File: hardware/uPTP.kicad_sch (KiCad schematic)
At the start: 1 part, among them U1 CH32V30xWxUx

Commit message: Key components
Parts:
- removed U1: CH32V30xWxUx, Package_DFN_QFN:QFN-68-1EP_8x8mm_P0.4mm_EP6.4x6.4mm, symbol MCU_WCH_CH32V3:CH32V30xWxUx
- added J1: USB_C_Receptacle_USB2.0_14P, symbol Connector:USB_C_Receptacle_USB2.0_14P
- added U1: CH32V307WCU6, uPTP:QFN-68_L8.0-W8.0-P0.40-BL-EP6.7, symbol uPTP:CH32V30xWxUx
- added U2: HC-RJ45-055-7, uPTP:RJ45-SMD_HC-RJ45-055-7_1, symbol uPTP:HC-RJ45-055-7
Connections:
- new net: J1.A1 (GND), J1.A12 (GND), J1.B1 (GND), J1.B12 (GND)
- new net: J1.A4 (VBUS), J1.A9 (VBUS), J1.B4 (VBUS), J1.B9 (VBUS)
- new net: U1.17 (VIO), U1.31 (VIO), U1.51 (VIO), U1.67 (VIO)
- new net: U1.18 (VSS), U1.49 (VSS), U1.69 (VSS)
- new net: U1.32 (VDD), U1.50 (VDD), U1.68 (VDD)
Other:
- note added: "TODO check exposed pad!"

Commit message: Some more handy components
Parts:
- removed J1: USB_C_Receptacle_USB2.0_14P, symbol Connector:USB_C_Receptacle_USB2.0_14P
- added D1: USBLC6-2SC6, uPTP:SOT-23-6_L2.9-W1.6-P0.95-LS2.8-BL, symbol uPTP:USBLC6-2SC6
- added J2: SMA, symbol Connector:Conn_Coaxial
- added J3: u.FL, symbol Connector:Conn_Coaxial_Small
- added USB1: TYPE-C 16PIN 2MD(073), uPTP:USB-C-SMD_TYPE-C-16PIN, symbol uPTP:USB-C-SMD_TYPE-C-16PIN
- added Y1: Crystal_GND2_Small, symbol Device:Crystal_GND2_Small
- U1: LCSC Part (none) -> C5142795
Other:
- note removed: "TODO check exposed pad!"
- moved on the sheet: U2

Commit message: Add magnetics
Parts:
- added TR1: ~, uPTP:B1608S, symbol uPTP:B1608S
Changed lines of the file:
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@@
+	)
+	(symbol
+		(lib_id "uPTP:B1608S")
+		(at 218.44 120.65 0)
+		(unit 1)
+		(exclude_from_sim no)
+		(in_bom yes)
+		(on_board yes)
+		(dnp no)
+		(property "Reference" "TR1"
+			(at 218.44 108.966 0)
+			(effects
+				(font
+					(size 1.27 1.27)
+				)
+			)
+		)
+		(property "Value" "~"
+			(at 218.44 109.22 0)
+			(effects
+				(font
+					(size 1.27 1.27)
+				)
+			)
+		)
+		(property "Footprint" "uPTP:B1608S"
+			(at 218.44 135.128 0)
+			(effects
+				(font
+					(size 1.27 1.27)
+				)
+				(hide yes)
+			)
+		)
+		(property "Datasheet" ""
+			(at 218.44 109.22 0)
+			(effects
+				(font
+					(size 1.27 1.27)
+				)
+				(hide yes)
+			)
+		)
+		(property "Description" "POE-Rated (720mA) Ethernet Magnetics"
+			(at 218.186 132.588 0)
+			(effects
+				(font
+					(size 1.27 1.27)
+				)
+				(hide yes)
+			)
+		)
+		(property "LCSC Part" "C507596"
+			(at 218.44 137.414 0)
+			(effects
+				(font
+					(size 1.27 1.27)
+				)
+				(hide yes)
+			)
+		)
+		(pin "6"
+		)
+		(pin "9"
+		)
+		(pin "8"
+		)
+		(pin "3"
+		)
+		(pin "11"
+		)
+		(pin "1"
+		)
+		(pin "10"
+		)
+		(pin "7"
+		)
+		(pin "2"
+		)
+		(pin "15"
+		)
+		(pin "14"
+		)
+		(pin "16"
+		)
+		(instances
+			(project ""
+				(path "/c29659fd-9e8d-4714-a690-4e74e6e849c2"
+					(reference "TR1")
+					(unit 1)
+				)
+			)
+		)
 	)
 	(symbol

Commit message: Nice first render
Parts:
- added H1, H2: MountingHole_Pad, MountingHole:MountingHole_3.2mm_M3_Pad, symbol Mechanical:MountingHole_Pad
- added J1: Conn_01x04_Pin, Connector_PinHeader_2.54mm:PinHeader_1x04_P2.54mm_Horizontal, symbol Connector:Conn_01x04_Pin
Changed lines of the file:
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@@
+	)
+	(symbol
+		(lib_id "Mechanical:MountingHole_Pad")
+		(at 107.95 179.07 0)
+		(unit 1)
+		(exclude_from_sim yes)
+		(in_bom no)
+		(on_board yes)
+		(dnp no)
+		(fields_autoplaced yes)
+		(property "Reference" "H1"
+			(at 110.49 176.5299 0)
+			(effects
+				(font
+					(size 1.27 1.27)
+				)
+				(justify left)
+			)
+		)
+		(property "Value" "MountingHole_Pad"
+			(at 110.49 179.0699 0)
+			(effects
+				(font
+					(size 1.27 1.27)
+				)
+				(justify left)
+			)
+		)
+		(property "Footprint" "MountingHole:MountingHole_3.2mm_M3_Pad"
+			(at 107.95 179.07 0)
+			(effects
+				(font
+					(size 1.27 1.27)
+				)
+				(hide yes)
+			)
+		)
+		(property "Datasheet" "~"
+			(at 107.95 179.07 0)
+			(effects
+				(font
+					(size 1.27 1.27)
+				)
+				(hide yes)
+			)
+		)
+		(property "Description" "Mounting Hole with connection"
+			(at 107.95 179.07 0)
+			(effects
+				(font
+					(size 1.27 1.27)
+				)
+				(hide yes)
+			)
+		)
+		(pin "1"
+		)
+		(instances
+			(project ""
+				(path "/c29659fd-9e8d-4714-a690-4e74e6e849c2"
+					(reference "H1")
+					(unit 1)
+				)
+			)
+		)
 	)
 	(symbol
@@
 	)
 	(symbol
+		(lib_id "Mechanical:MountingHole_Pad")
+		(at 127 179.07 0)
+		(unit 1)
+		(exclude_from_sim yes)
+		(in_bom no)
+		(on_board yes)
+		(dnp no)
+		(fields_autoplaced yes)
+		(property "Reference" "H2"
+			(at 129.54 176.5299 0)
+			(effects
+				(font
+					(size 1.27 1.27)
+				)
+				(justify left)
+			)
+		)
+		(property "Value" "MountingHole_Pad"
+			(at 129.54 179.0699 0)
+			(effects
+				(font
+					(size 1.27 1.27)
+				)
+				(justify left)
+			)
+		)
+		(property "Footprint" "MountingHole:MountingHole_3.2mm_M3_Pad"
+			(at 127 179.07 0)
+			(effects
+				(font
+					(size 1.27 1.27)
+				)
+				(hide yes)
+			)
+		)
+		(property "Datasheet" "~"
+			(at 127 179.07 0)
+			(effects
+				(font
+					(size 1.27 1.27)
+				)
+				(hide yes)
+			)
+		)
+		(property "Description" "Mounting Hole with connection"
+			(at 127 179.07 0)
+			(effects
+				(font
+					(size 1.27 1.27)
+				)
+				(hide yes)
+			)
+		)
+		(pin "1"
+		)
+		(instances
+			(project "uPTP"
+				(path "/c29659fd-9e8d-4714-a690-4e74e6e849c2"
+					(reference "H2")
+					(unit 1)
+				)
+			)
+		)
+	)
+	(symbol
 		(lib_id "uPTP:USBLC6-2SC6")
 		(at 80.01 74.93 0)
@@
 					(unit 1)
 				)
+			)
+		)
+	)
+	(symbol
+		(lib_id "Connector:Conn_01x04_Pin")
+		(at 45.72 123.19 0)
+		(unit 1)
+		(exclude_from_sim no)
+		(in_bom yes)
+		(on_board yes)
+		(dnp no)
+		(fields_autoplaced yes)
+		(property "Reference" "J1"
+			(at 46.355 115.57 0)
+			(effects
+				(font
+					(size 1.27 1.27)
+				)
+			)
+		)
+		(property "Value" "Conn_01x04_Pin"
+			(at 46.355 118.11 0)
+			(effects
+				(font
+					(size 1.27 1.27)
+				)
+			)
+		)
+		(property "Footprint" "Connector_PinHeader_2.54mm:PinHeader_1x04_P2.54mm_Horizontal"
+			(at 45.72 123.19 0)
+			(effects
+				(font
+					(size 1.27 1.27)
+				)
+				(hide yes)
+			)
+		)
+		(property "Datasheet" "~"
+			(at 45.72 123.19 0)
+			(effects
+				(font
+					(size 1.27 1.27)
+				)
+				(hide yes)
+			)
+		)
+		(property "Description" "Generic connector, single row, 01x04, script generated"
+			(at 45.72 123.19 0)
+			(effects
+				(font
+					(size 1.27 1.27)
+				)
+				(hide yes)
+			)
+		)
+		(pin "4"
+		)
+		(pin "1"
+		)
+		(pin "2"
+		)
+		(pin "3"
+		)
+		(instances
+			(project ""
+				(path "/c29659fd-9e8d-4714-a690-4e74e6e849c2"
+					(reference "J1")
+					(unit 1)
+				)

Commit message: POE CTRL?
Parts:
- added D2: D_Schottky, symbol Device:D_Schottky
- added U3: TMI7301, uPTP:SOP-8_L4.9-W3.9-P1.27-LS6.0-TL, symbol uPTP:TMI7301
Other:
- moved on the sheet: J1, TR1, U1, U2, Y1
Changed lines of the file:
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@@
 	(symbol
 		(lib_id "uPTP:HC-RJ45-055-7")
-		(at 247.65 120.65 0)
+		(at 36.83 152.4 0)
+		(mirror y)
 		(unit 1)
 		(exclude_from_sim no)
@@
 		(on_board yes)
 		(dnp no)
-		(fields_autoplaced yes)
 		(property "Reference" "U2"
-			(at 257.81 119.3799 0)
+			(at 26.67 151.1299 0)
 			(effects
 				(font
@@
 		)
 		(property "Value" "HC-RJ45-055-7"
-			(at 257.81 121.9199 0)
+			(at 26.67 153.6699 0)
 			(effects
 				(font
@@
 		)
 		(property "Footprint" "uPTP:RJ45-SMD_HC-RJ45-055-7_1"
-			(at 247.65 142.24 0)
+			(at 36.83 173.99 0)
 			(effects
 				(font
@@
 		)
 		(property "Datasheet" ""
-			(at 241.3 120.65 0)
+			(at 43.18 152.4 0)
 			(effects
 				(font
@@
 		)
 		(property "Description" "Half-Recessed SMD RJ45 Connector"
-			(at 241.3 120.65 0)
+			(at 43.18 152.4 0)
 			(effects
 				(font
@@
 		)
 		(property "LCSC Part" "C3000213"
-			(at 247.65 144.78 0)
+			(at 36.83 176.53 0)
 			(effects
 				(font
@@
 	(symbol
 		(lib_id "Device:Crystal_GND2_Small")
-		(at 185.42 57.15 0)
+		(at 193.04 97.79 0)
 		(unit 1)
 		(exclude_from_sim no)
@@
 		(fields_autoplaced yes)
 		(property "Reference" "Y1"
-			(at 185.42 50.8 0)
+			(at 193.04 91.44 0)
 			(effects
 				(font
@@
 		)
 		(property "Value" "Crystal_GND2_Small"
-			(at 185.42 53.34 0)
+			(at 193.04 93.98 0)
 			(effects
 				(font
@@
 		)
 		(property "Footprint" ""
-			(at 185.42 57.15 0)
+			(at 193.04 97.79 0)
 			(effects
 				(font
@@
 		)
 		(property "Datasheet" "~"
-			(at 185.42 57.15 0)
+			(at 193.04 97.79 0)
 			(effects
 				(font
@@
 		)
 		(property "Description" "Three pin crystal, GND on pin 2, small symbol"
-			(at 185.42 57.15 0)
+			(at 193.04 97.79 0)
 			(effects
 				(font
@@
 	(symbol
 		(lib_id "uPTP:B1608S")
-		(at 218.44 120.65 0)
+		(at 62.23 152.4 0)
 		(unit 1)
 		(exclude_from_sim no)
@@
 		(dnp no)
 		(property "Reference" "TR1"
-			(at 218.44 108.966 0)
+			(at 62.23 140.716 0)
 			(effects
 				(font
@@
 		)
 		(property "Value" "~"
-			(at 218.44 109.22 0)
+			(at 62.23 140.97 0)
 			(effects
 				(font
@@
 		)
 		(property "Footprint" "uPTP:B1608S"
-			(at 218.44 135.128 0)
+			(at 62.23 166.878 0)
 			(effects
 				(font
@@
 		)
 		(property "Datasheet" ""
-			(at 218.44 109.22 0)
+			(at 62.23 140.97 0)
 			(effects
 				(font
@@
 		)
 		(property "Description" "POE-Rated (720mA) Ethernet Magnetics"
-			(at 218.186 132.588 0)
+			(at 61.976 164.338 0)
 			(effects
 				(font
@@
 		)
 		(property "LCSC Part" "C507596"
-			(at 218.44 137.414 0)
+			(at 62.23 169.164 0)
 			(effects
 				(font
@@
 	(symbol
 		(lib_id "uPTP:CH32V30xWxUx")
-		(at 140.97 106.68 0)
+		(at 152.4 87.63 0)
 		(unit 1)
 		(exclude_from_sim no)
@@
 		(fields_autoplaced yes)
 		(property "Reference" "U1"
-			(at 153.3241 157.48 0)
+			(at 164.7541 138.43 0)
 			(effects
 				(font
@@
 		)
 		(property "Value" "CH32V307WCU6"
-			(at 153.3241 160.02 0)
+			(at 164.7541 140.97 0)
 			(effects
 				(font
@@
 		)
 		(property "Footprint" "uPTP:QFN-68_L8.0-W8.0-P0.40-BL-EP6.7"
-			(at 140.97 101.6 0)
+			(at 152.4 82.55 0)
 			(effects
 				(font
@@
 		)
 		(property "Datasheet" "http://www.wch-ic.com/products/CH32V307.html?"
-			(at 140.97 111.76 0)
+			(at 152.4 92.71 0)
 			(effects
 				(font
@@
 		)
 		(property "Description" "The CH32V303/5/7 is an connectivity MCUs based on 32-bit RISC-V core."
-			(at 140.97 106.68 0)
+			(at 152.4 87.63 0)
 			(effects
 				(font
@@
 		)
 		(property "LCSC Part" "C5142795"
-			(at 140.716 181.356 0)
+			(at 152.146 162.306 0)
 			(effects
 				(font
@@
 	)
 	(symbol
+		(lib_id "Device:D_Schottky")
+		(at 67.31 55.88 180)
+		(unit 1)
+		(exclude_from_sim no)
+		(in_bom yes)
+		(on_board yes)
+		(dnp no)
+		(fields_autoplaced yes)
+		(property "Reference" "D2"
+			(at 67.6275 49.53 0)
+			(effects
+				(font
+					(size 1.27 1.27)
+				)
+			)
+		)
+		(property "Value" "D_Schottky"
+			(at 67.6275 52.07 0)
+			(effects
+				(font
+					(size 1.27 1.27)
+				)
+			)
+		)
+		(property "Footprint" ""
+			(at 67.31 55.88 0)
+			(effects
+				(font
+					(size 1.27 1.27)
+				)
+				(hide yes)
+			)
+		)
+		(property "Datasheet" "~"
+			(at 67.31 55.88 0)
+			(effects
+				(font
+					(size 1.27 1.27)
+				)
+				(hide yes)
+			)
+		)
+		(property "Description" "Schottky diode"
+			(at 67.31 55.88 0)
+			(effects
+				(font
+					(size 1.27 1.27)
+				)
+				(hide yes)
+			)
+		)
+		(pin "2"
+		)
+		(pin "1"
+		)
+		(instances
+			(project ""
+				(path "/c29659fd-9e8d-4714-a690-4e74e6e849c2"
+					(reference "D2")
+					(unit 1)
+				)
+			)
+		)
+	)
+	(symbol
 		(lib_id "uPTP:USB-C-SMD_TYPE-C-16PIN")
 		(at 40.64 76.2 0)
@@
 	)
 	(symbol
+		(lib_id "uPTP:TMI7301")
+		(at 87.63 151.13 0)
+		(unit 1)
+		(exclude_from_sim no)
+		(in_bom yes)
+		(on_board yes)
+		(dnp no)
+		(fields_autoplaced yes)
+		(property "Reference" "U3"
+			(at 89.8241 135.89 0)
+			(effects
+				(font
+					(size 1.27 1.27)
+				)
+				(justify left)
+			)
+		)
+		(property "Value" "TMI7301"
+			(at 89.8241 138.43 0)
+			(effects
+				(font
+					(size 1.27 1.27)
+				)
+				(justify left)
+			)
+		)
+		(property "Footprint" "uPTP:SOP-8_L4.9-W3.9-P1.27-LS6.0-TL"
+			(at 87.63 177.8 0)
+			(effects
+				(font
+					(size 1.27 1.27)
+				)
+				(hide yes)
+			)
+		)
+		(property "Datasheet" ""
+			(at 87.63 149.86 0)
+			(effects
+				(font
+					(size 1.27 1.27)
+				)
+				(hide yes)
+			)
+		)
+		(property "Description" "POE 802.3af Controller IC"
+			(at 87.63 182.626 0)
+			(effects
+				(font
+					(size 1.27 1.27)
+				)
+				(hide yes)
+			)
+		)
+		(property "LCSC Part" "C29779858"
+			(at 87.63 180.34 0)
+			(effects
+				(font
+					(size 1.27 1.27)
+				)
+				(hide yes)
+			)
+		)
+		(pin "5"
+		)
+		(pin "7"
+		)
+		(pin "6"
+		)
+		(pin "1"
+		)
+		(pin "8"
+		)
+		(pin "2"
+		)
+		(pin "3"
+		)
+		(pin "4"
+		)
+		(instances
+			(project ""
+				(path "/c29659fd-9e8d-4714-a690-4e74e6e849c2"
+					(reference "U3")
+					(unit 1)
+				)
+			)
+		)
+	)
+	(symbol
 		(lib_id "uPTP:USBLC6-2SC6")
 		(at 80.01 74.93 0)
@@
 	(symbol
 		(lib_id "Connector:Conn_01x04_Pin")
-		(at 45.72 123.19 0)
+		(at 236.22 130.81 0)
 		(unit 1)
 		(exclude_from_sim no)
@@
 		(fields_autoplaced yes)
 		(property "Reference" "J1"
-			(at 46.355 115.57 0)
+			(at 236.855 123.19 0)
 			(effects
 				(font
@@
 		)
 		(property "Value" "Conn_01x04_Pin"
-			(at 46.355 118.11 0)
+			(at 236.855 125.73 0)
 			(effects
 				(font
@@
 		)
 		(property "Footprint" "Connector_PinHeader_2.54mm:PinHeader_1x04_P2.54mm_Horizontal"
-			(at 45.72 123.19 0)
+			(at 236.22 130.81 0)
 			(effects
 				(font
@@
 		)
 		(property "Datasheet" "~"
-			(at 45.72 123.19 0)
+			(at 236.22 130.81 0)
 			(effects
 				(font
@@
 		)
 		(property "Description" "Generic connector, single row, 01x04, script generated"
-			(at 45.72 123.19 0)
-			(effects
-				(font
+			(at 236.22 130.81 0)
+			(effects
+				(font

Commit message: Backup progress
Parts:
- removed TR1: ~, uPTP:B1608S, symbol uPTP:B1608S
- removed U2: HC-RJ45-055-7, uPTP:RJ45-SMD_HC-RJ45-055-7_1, symbol uPTP:HC-RJ45-055-7
- removed U3: TMI7301, uPTP:SOP-8_L4.9-W3.9-P1.27-LS6.0-TL, symbol uPTP:TMI7301
- added C4: 100n, Capacitor_SMD:C_0402_1005Metric, symbol Device:C
- added JP1: POE_ENABLE, symbol Jumper:Jumper_2_Small_Bridged
- added R1, R2: 5.1k, Resistor_SMD:R_0402_1005Metric, symbol Device:R
- added R10, R7, R8, R9: 49.9, Resistor_SMD:R_0402_1005Metric, symbol Device:R
- D1: renamed from D2; footprint (none) -> Diode_SMD:D_SOD-323; LCSC Part (none) -> C133103
- renumbered D1 to D2, J3 to J2, J2 to J3
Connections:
- net GND: now reaches USB1.1 (GND)
- net GND: now also D2.2 (GND), USB1.12 (GND), USB1.13 (SHELL), R1.2, R2.2
- net at USB1.10 (CC2): now also R1.1
- net +5V_USB: now reaches USB1.11 (VBUS)
- net +5V_USB: now also USB1.2 (VBUS), C4.1
- net at USB1.4 (CC1): now also R2.1
- net USB_D_CONN_N: now reaches USB1.5 (DN2)
- net USB_D_CONN_N: now also D2.1 (I/O1), USB1.7 (DN1)
- net USB_D_CONN_P: now reaches USB1.6 (DP1)
- net USB_D_CONN_P: now also D2.3 (I/O2), USB1.8 (DP2)
- net USB_D_P: now reaches D2.4 (I/O2)
- net at D2.5 (VBUS): now also C4.2
- net USB_D_N: now reaches D2.6 (I/O1)
- new net Ethernet and POE/V_POE: JP1.1 (A)
- no-connect marks 0 -> 2
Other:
- added sheet Ethernet and POE (ethernet.kicad_sch)
- added sheet Power (power.kicad_sch)
- note added: "Unsure if Phy has built-in termination"
- moved on the sheet: D1, U1, USB1, Y1

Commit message: Vaguely convincing render...
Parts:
- removed J2: u.FL, symbol Connector:Conn_Coaxial_Small
- removed R10, R7, R8, R9: 49.9, Resistor_SMD:R_0402_1005Metric, symbol Device:R
- added J2: PPS_UFL, uPTP:IPEX-SMD_HC-RF-IPEX0303-01, symbol uPTP:Conn_Coaxial_Small
- J3: value SMA -> PPS_SMA; footprint (none) -> Connector_Coaxial:SMA_Samtec_SMA-J-P-H-ST-EM1_EdgeMount
- JP1: footprint (none) -> Jumper:SolderJumper-2_P1.3mm_Bridged_RoundedPad1.0x1.5mm
- renumbered C4 to C1
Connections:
- net +5V_USB: now also D2.5 (VBUS)
- net GND: now also C1.2
- net Power/V_POE: now reaches JP1.2 (B)
- no-connect marks 2 -> 4
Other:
- sheet Ethernet and POE ports: added POE_READY; removed none
- sheet Power ports: added V_3V3, V_5V, V_AUX, V_POE, V_USB; removed none
- note removed: "Unsure if Phy has built-in termination"
- moved on the sheet: C1, D1, H1, H2, J3, JP1

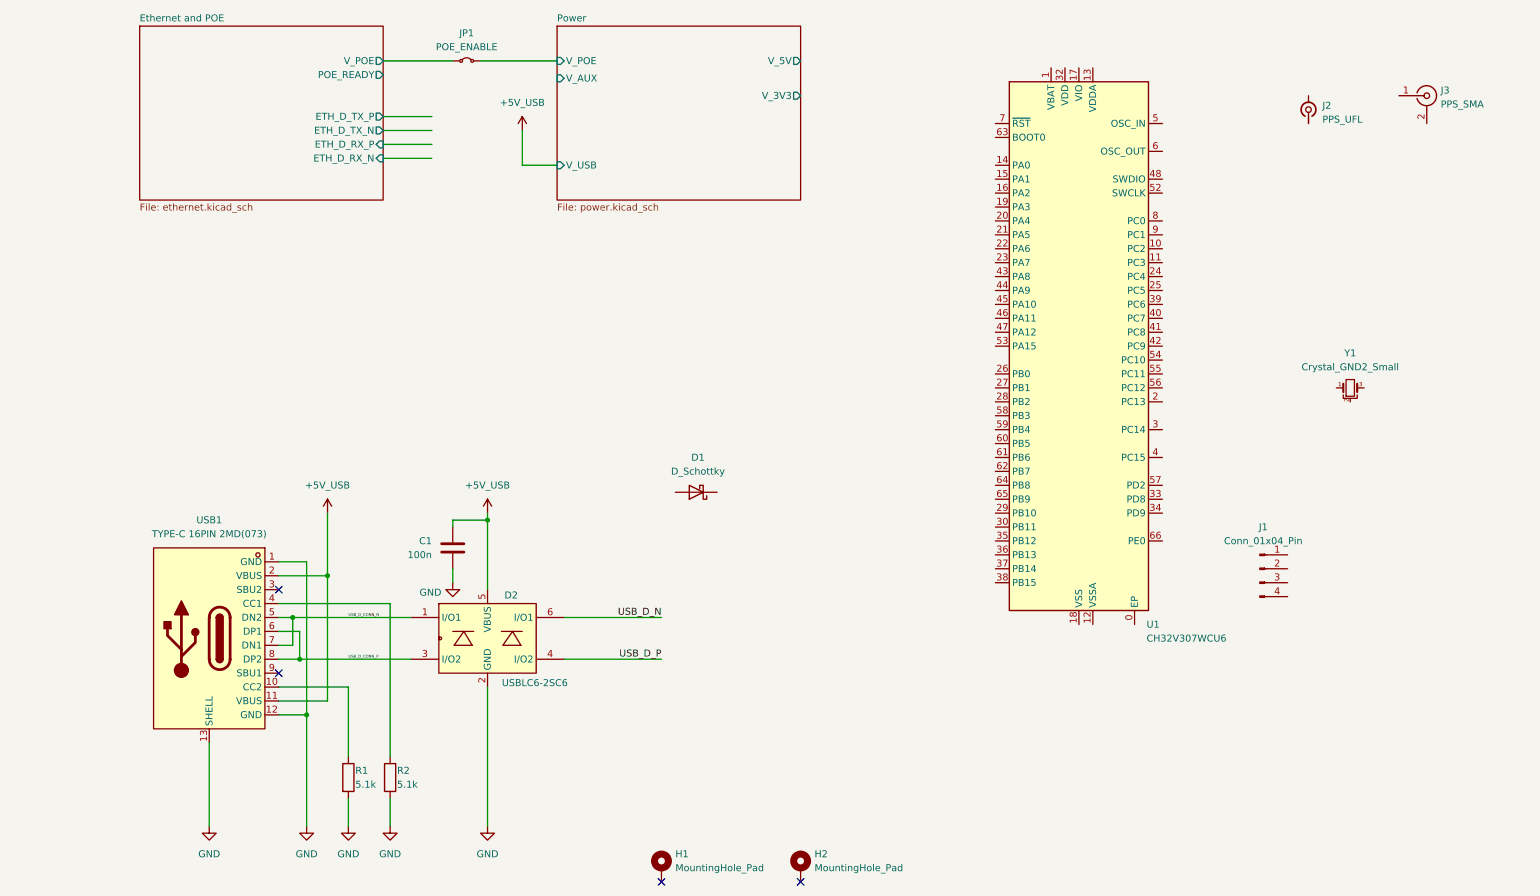
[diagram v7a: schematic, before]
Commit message: Component selection mostly done
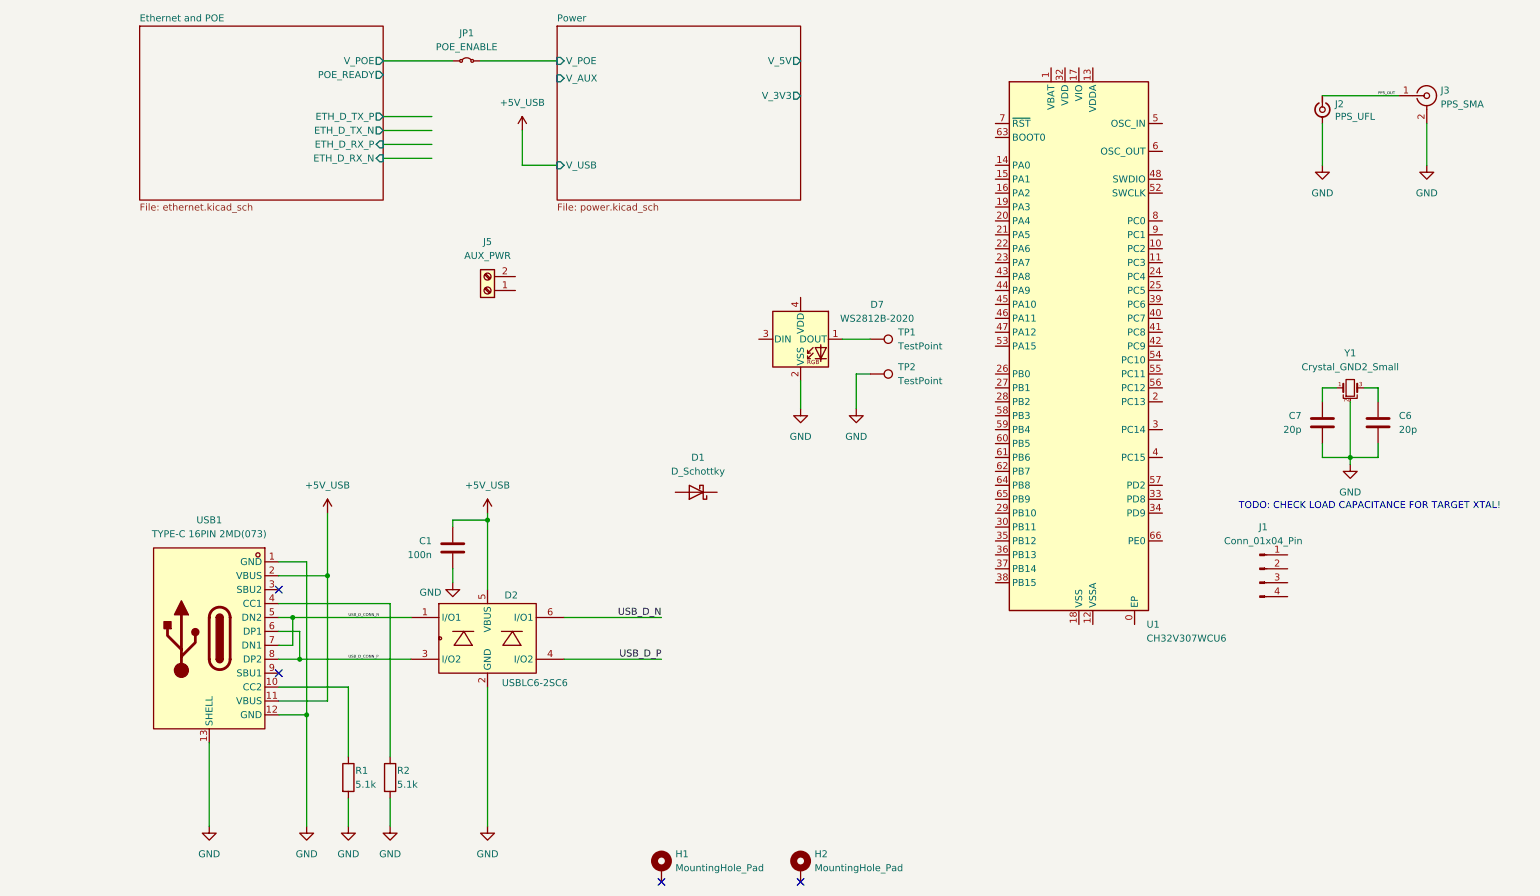
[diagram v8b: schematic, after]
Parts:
- added C6, C7: 20p, Capacitor_SMD:C_0402_1005Metric, symbol Device:C
- added D7: WS2812B-2020, LED_SMD:LED_WS2812B-2020_PLCC4_2.0x2.0mm, symbol LED:WS2812B-2020
- added J5: AUX_PWR, TerminalBlock_Phoenix:TerminalBlock_Phoenix_MPT-0,5-2-2.54_1x02_P2.54mm_Horizontal, symbol Connector:Screw_Terminal_01x02
- added TP1, TP2: TestPoint, symbol Connector:TestPoint
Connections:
- net GND: now also J2.2 (Ext), J3.2 (Ext), Y1.2, C6.2, C7.2, D7.2 (VSS), TP2.1
- net at Y1.1: now also C7.1
- net at Y1.3: now also C6.1
- net PPS_OUT: now reaches J2.1 (In)
- net PPS_OUT: now also J3.1 (In)
- new net: D7.1 (DOUT), TP1.1
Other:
- note added: "TODO: CHECK LOAD CAPACITANCE FOR TARGET XTAL!"
- moved on the sheet: J2
